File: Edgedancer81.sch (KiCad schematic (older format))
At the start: 30 parts

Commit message: more wires
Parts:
- added D? (x16): D_Small, symbol Device:D_Small
- added MX? (x4): MX-NoLED, symbol MX_Alps_Hybrid:MX-NoLED
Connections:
- net at D?.1 (K): now also D?.1 (K), D?.1 (K), D?.1 (K), D?.1 (K), D?.1 (K), D?.1 (K), D?.1 (K), D?.1 (K), D?.1 (K), D?.1 (K), D?.1 (K), D?.1 (K), D?.1 (K), D?.1 (K), D?.1 (K), D?.1 (K)
- net at MX?.2 (ROW): now also D?.2 (A) (x12)
- new net: D?.2 (A), MX?.2 (ROW) (x4)
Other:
- moved on the sheet: D?, MX?

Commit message: traces
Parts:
- removed D? (x17): D_Small, symbol Device:D_Small
- removed MX? (x17): MX-NoLED, symbol MX_Alps_Hybrid:MX-NoLED
- added SW2: Rotary_Encoder_Switch, Rotary_Encoder:RotaryEncoder_Alps_EC11E-Switch_Vertical_H20mm, symbol Device:Rotary_Encoder_Switch
- C1, C2, C3, C4, C5, C6, C7: renamed from C?; footprint (none) -> Capacitor_SMD:C_0805_2012Metric
- F1: renamed from F?; footprint (none) -> Fuse:Fuse_1206_3216Metric
- R1, R2, R3, R4: renamed from R?; footprint (none) -> Resistor_SMD:R_0805_2012Metric
- SW1: renamed from SW?; footprint (none) -> random-keyboard-parts:SKQG-1155865
- USB1: renamed from USB?; footprint (none) -> random-keyboard-parts:Molex-0548190589
- Y1: renamed from Y?; footprint (none) -> Crystal:Crystal_SMD_3225-4Pin_3.2x2.5mm
- gave numbers to parts that had none: 1
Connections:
- net GND: now also SW2.C, SW2.S2
- net ROW_2: now reaches U1.10 (PB2)
- net ROW_1: now reaches U1.11 (PB3)
- net ROW_0: now reaches U1.12 (PB7)
- net ENC_A: now reaches U1.18 (PD0)
- net ENC_A: now also SW2.A
- net ENC_B: now reaches U1.19 (PD1)
- net ENC_B: now also SW2.B
- net COL_7: now reaches U1.20 (PD2)
- net COL_8: now reaches U1.21 (PD3)
- net COL_0: now reaches U1.22 (PD5)
- net ENC_SW: now reaches U1.25 (PD4)
- net ENC_SW: now also SW2.S1
- net ROW_10: now reaches U1.26 (PD6)
- net ROW_11: now reaches U1.27 (PD7)
- net ROW_9: now reaches U1.28 (PB4)
- net ROW_8: now reaches U1.29 (PB5)
- net ROW_7: now reaches U1.30 (PB6)
- net ROW_6: now reaches U1.31 (PC6)
- net ROW_5: now reaches U1.32 (PC7)
- net COL_1: now reaches U1.36 (PF7)
- net COL_2: now reaches U1.37 (PF6)
- net COL_3: now reaches U1.38 (PF5)
- net COL_4: now reaches U1.39 (PF4)
- net COL_5: now reaches U1.40 (PF1)
- net COL_6: now reaches U1.41 (PF0)
- net ROW_4: now reaches U1.8 (PB0)
- net ROW_3: now reaches U1.9 (PB1)

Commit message: silkscreen and bugfixes
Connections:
- net ROW_10: now also U1.27 (PD7); no longer U1.26 (PD6)
- net ROW_11: now also U1.26 (PD6); no longer U1.27 (PD7)
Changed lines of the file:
@@
 Text GLabel 4050 4000 2    50   Input ~ 0
 ROW_8
+Text GLabel 4050 5400 2    50   Input ~ 0
+ROW_10
 Text GLabel 4050 5300 2    50   Input ~ 0
-ROW_10
-Text GLabel 4050 5400 2    50   Input ~ 0
 ROW_11
 Text GLabel 4050 5100 2    50   Input ~ 0

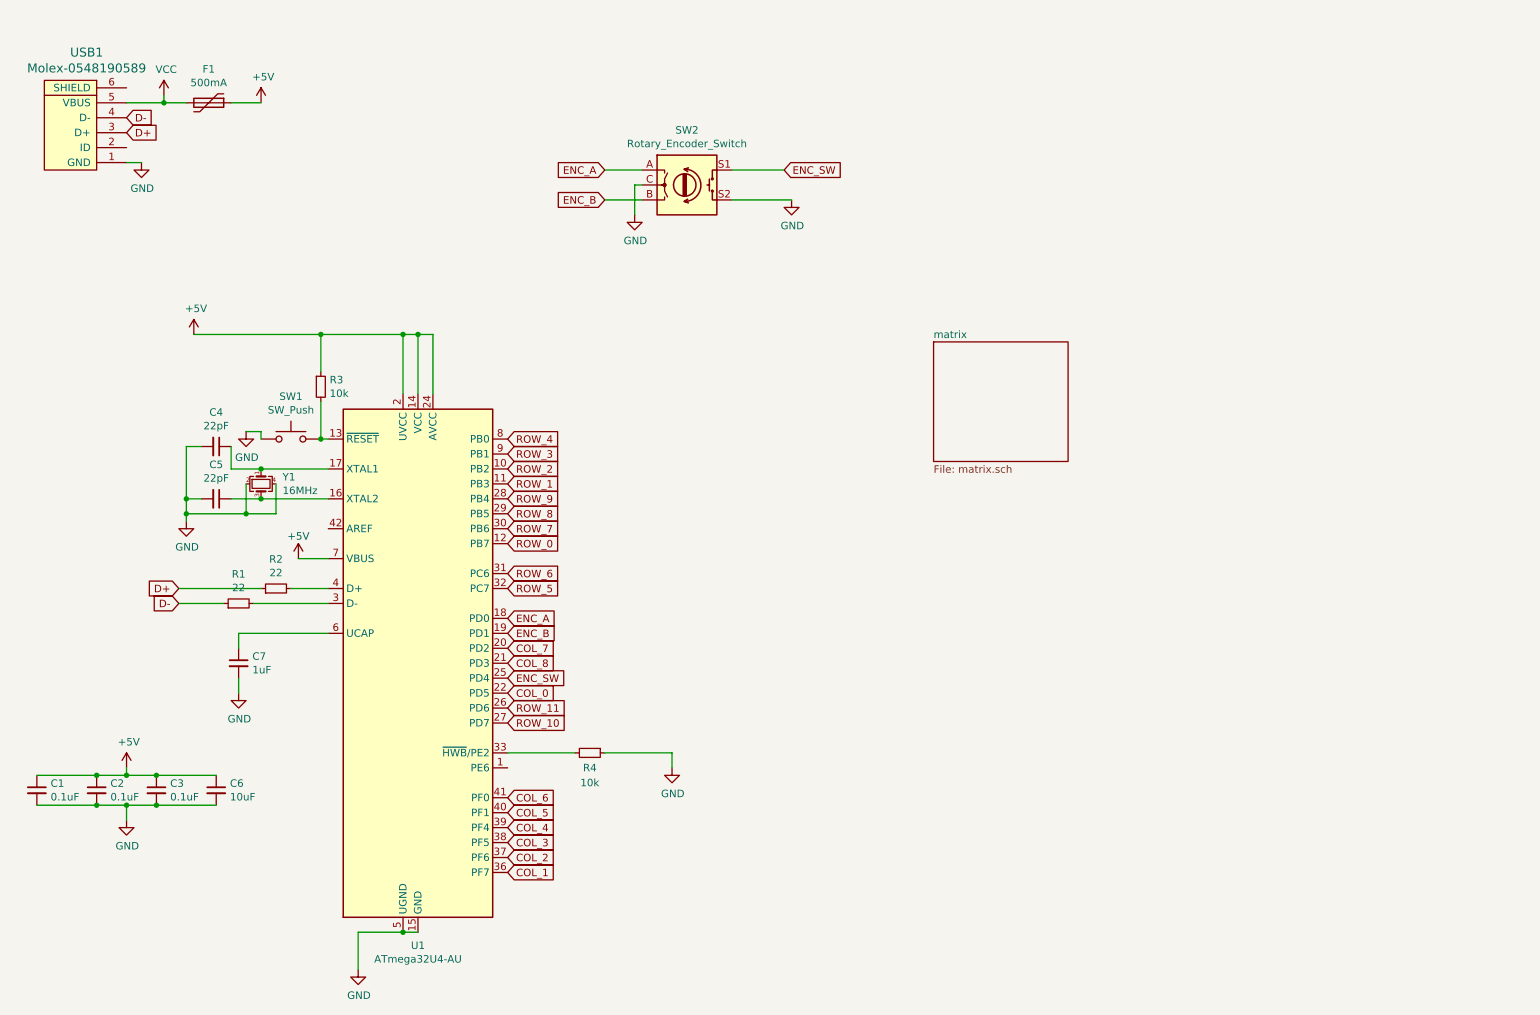
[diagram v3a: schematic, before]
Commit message: Updated for type-c
Still needs to update the pcb
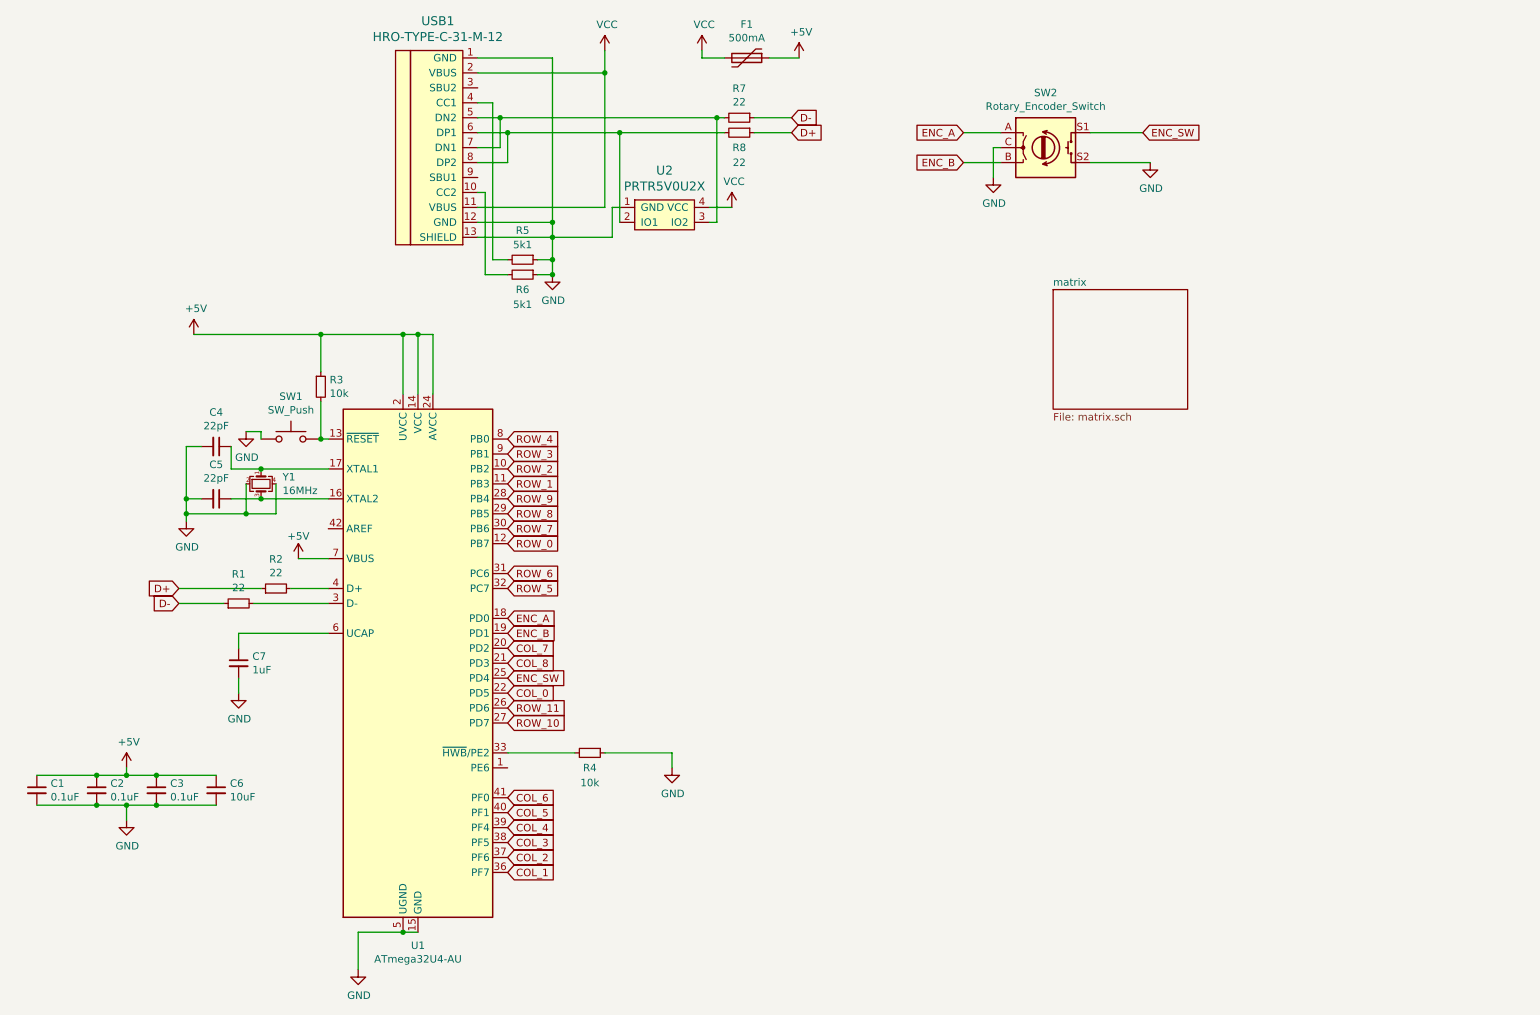
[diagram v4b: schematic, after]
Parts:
- removed USB1: Molex-0548190589, random-keyboard-parts:Molex-0548190589, symbol random-keyboard-parts:Molex-0548190589
- added R5, R6: 5k1, Resistor_SMD:R_0805_2012Metric, symbol Device:R_Small
- added R7, R8: 22, Resistor_SMD:R_0805_2012Metric, symbol Device:R_Small
- added U2: PRTR5V0U2X, random-keyboard-parts:SOT143B, symbol random-keyboard-parts:PRTR5V0U2X
- added USB1: HRO-TYPE-C-31-M-12, Type-C:HRO-TYPE-C-31-M-12-Assembly, symbol Type-C:HRO-TYPE-C-31-M-12
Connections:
- net D+: now also R8.1
- net D-: now also R7.1
- net GND: now also R5.1, R6.1, U2.1 (GND), USB1.1 (GND), USB1.12 (GND), USB1.13 (SHIELD)
- net VCC: now also U2.4 (VCC), USB1.11 (VBUS), USB1.2 (VBUS)
- new net: R6.2, USB1.10 (CC2)
- new net: R5.2, USB1.4 (CC1)
- new net: R7.2, U2.3 (IO2), USB1.5 (DN2), USB1.7 (DN1)
- new net: R8.2, U2.2 (IO1), USB1.6 (DP1), USB1.8 (DP2)
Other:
- moved on the sheet: SW2

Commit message: Finished traces
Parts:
- removed R1, R2: 22, Resistor_SMD:R_0805_2012Metric, symbol Device:R_Small
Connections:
- net D+: now also U1.4 (D+)
- net D-: now also U1.3 (D-)
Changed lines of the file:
@@
 	4050 5600 4500 5600
-$Comp
-L Device:R_Small R2
-U 1 1 5F0E6918
-P 2500 4500
-F 0 "R2" V 2696 4500 50  0000 C CNN
-F 1 "22" V 2605 4500 50  0000 C CNN
-F 2 "Resistor_SMD:R_0805_2012Metric" H 2500 4500 50  0001 C CNN
-F 3 "~" H 2500 4500 50  0001 C CNN
-	1    2500 4500
-	0    -1   -1   0
-$EndComp
-Wire Wire Line
-	2600 4500 2850 4500
-$Comp
-L Device:R_Small R1
-U 1 1 5F0E9BF6
-P 2250 4600
-F 0 "R1" V 2446 4600 50  0000 C CNN
-F 1 "22" V 2355 4600 50  0000 C CNN
-F 2 "Resistor_SMD:R_0805_2012Metric" H 2250 4600 50  0001 C CNN
-F 3 "~" H 2250 4600 50  0001 C CNN
-	1    2250 4600
-	0    -1   -1   0
-$EndComp
-Wire Wire Line
-	2350 4600 2850 4600
-Wire Wire Line
-	2400 4500 1850 4500
-Wire Wire Line
-	2150 4600 1850 4600
 $Comp
 L Device:C_Small C7
@@
 Wire Wire Line
 	5350 950  5500 950
+Wire Wire Line
+	1850 4600 2850 4600
+Wire Wire Line
+	1850 4500 2850 4500
 $EndSCHEMATC

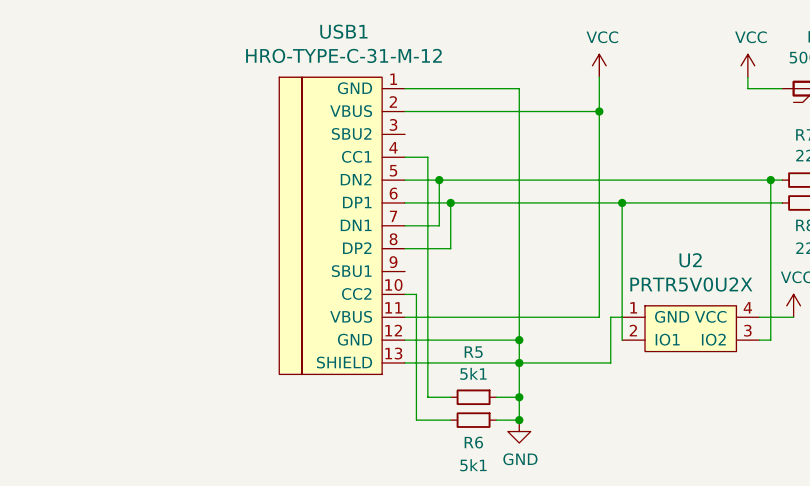
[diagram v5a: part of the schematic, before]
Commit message: cleaned up data traces
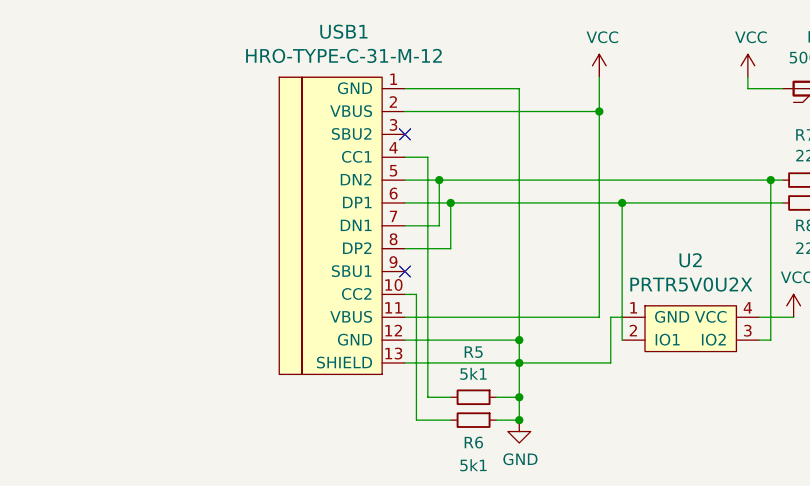
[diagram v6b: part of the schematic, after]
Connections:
- no-connect marks 0 -> 2
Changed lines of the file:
@@
 Wire Wire Line
 	1850 4500 2850 4500
+NoConn ~ 3850 1750
+NoConn ~ 3850 1150
 $EndSCHEMATC
